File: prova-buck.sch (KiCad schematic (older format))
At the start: 23 parts

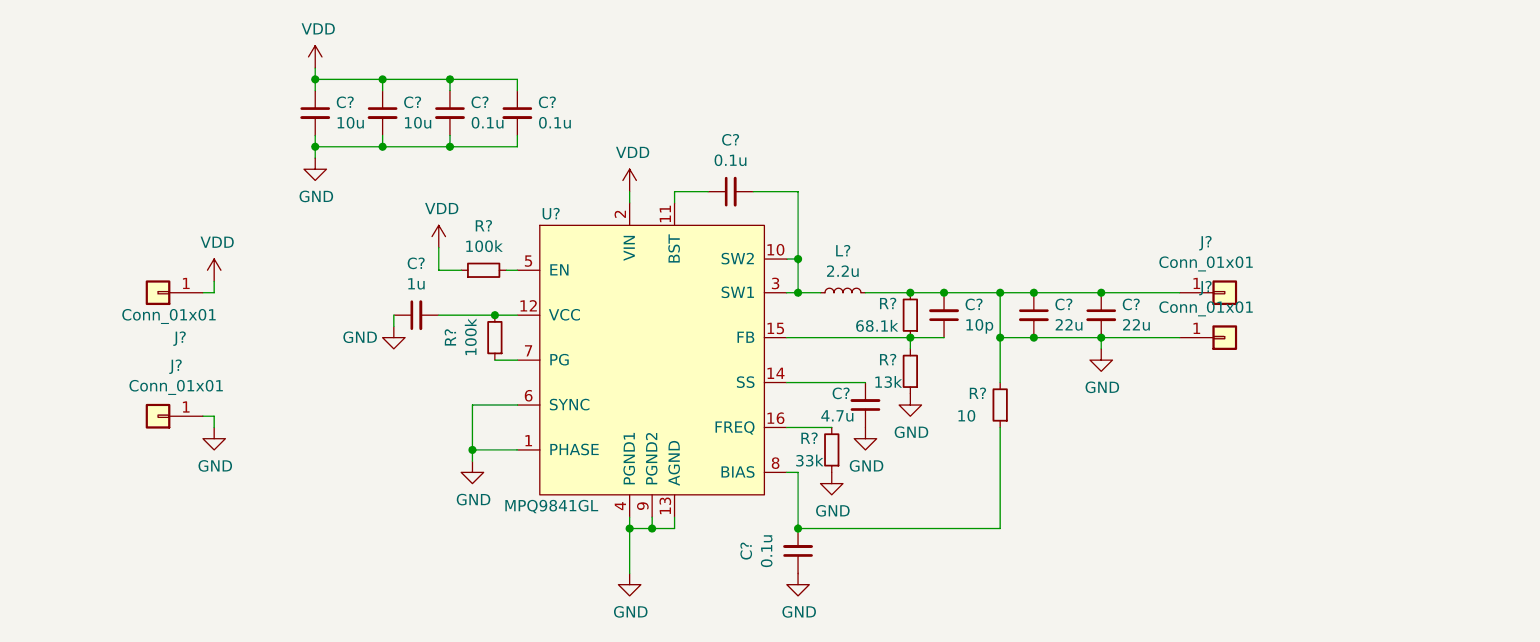
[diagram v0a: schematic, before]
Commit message: Added footprints
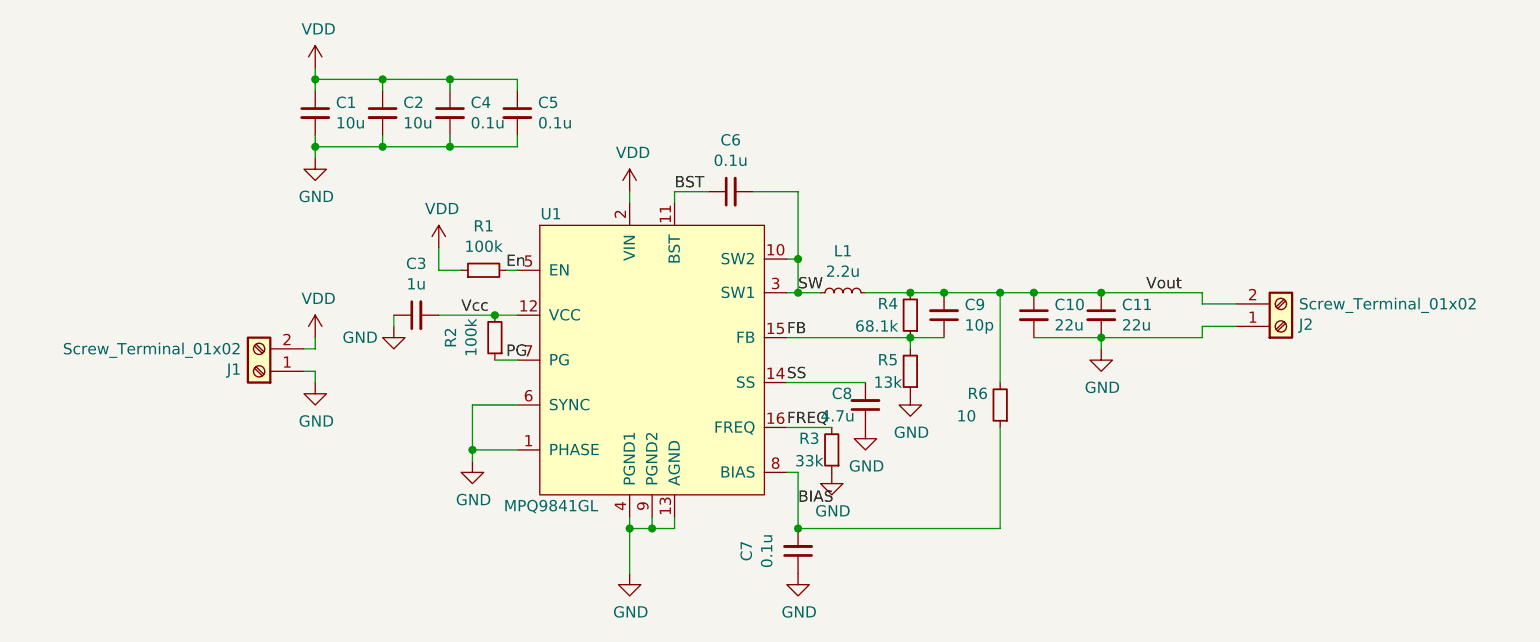
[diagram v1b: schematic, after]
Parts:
- removed J? (x4): Conn_01x01, symbol Connector_Generic:Conn_01x01
- added J1, J2: Screw_Terminal_01x02, TerminalBlock:TerminalBlock_bornier-2_P5.08mm, symbol Connector:Screw_Terminal_01x02
- C1, C2: renamed from C?; footprint (none) -> Capacitor_SMD:C_1206_3216Metric
- C10, C11: renamed from C?; footprint (none) -> Capacitor_SMD:C_0805_2012Metric
- C3, C4, C5, C6, C7, C8, C9: renamed from C?; footprint (none) -> Capacitor_SMD:C_0603_1608Metric
- L1: renamed from L?; footprint (none) -> Inductor_SMD:L_Sunlord_MWSA0518_5.4x5.2mm
- R1, R2, R3, R4, R5, R6: renamed from R?; footprint (none) -> Resistor_SMD:R_0603_1608Metric
- U1: renamed from U?; footprint (none) -> buck_foot_lib:QFN16_3mm_x_4mm
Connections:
- net GND: now also J1.1 (Pin_1), J2.1 (Pin_1); no longer C10.1, C11.1, C9.2, L1.2, R4.2, R6.2
- net VDD: now also J1.2 (Pin_2)
- net SW: now reaches C6.2, L1.1, U1.10 (SW2), U1.3 (SW1)
- net BST: now reaches C6.1, U1.11 (BST)
- net Vcc: now reaches C3.2, R2.2, U1.12 (VCC)
- net SS: now reaches C8.2, U1.14 (SS)
- net FB: now reaches C9.1, R4.1, R5.2, U1.15 (FB)
- net FREQ: now reaches R3.2, U1.16 (FREQ)
- net En: now reaches R1.2, U1.5 (EN)
- net PG: now reaches R2.1, U1.7 (PG)
- net BIAS: now reaches C7.2, R6.1, U1.8 (BIAS)
- new net Vout: C10.1, C11.1, C9.2, J2.2 (Pin_2), L1.2, R4.2, R6.2
